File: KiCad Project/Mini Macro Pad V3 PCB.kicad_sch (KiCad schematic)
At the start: 0 parts

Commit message: added basic components & neopixels to schematic
just adding base components to schematic. not really any wiring yet
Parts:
- added D1, D10, D2, D3, D4, D5, D6, D7, D8, D9: NeoPixel_THT, symbol LED:NeoPixel_THT
- added J1: USB_C_Receptacle_USB2.0_14P, symbol Connector:USB_C_Receptacle_USB2.0_14P
- added U1: RP2040, Package_DFN_QFN:QFN-56-1EP_7x7mm_P0.4mm_EP3.2x3.2mm, symbol MCU_RaspberryPi:RP2040
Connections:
- new net: D8.1 (DOUT), D9.4 (DIN)
- new net: D7.1 (DOUT), D8.4 (DIN)
- new net: D2.1 (DOUT), D3.4 (DIN)
- new net: D1.1 (DOUT), D2.4 (DIN)
- new net: D10.1 (DOUT), D7.4 (DIN)
- new net: D4.1 (DOUT), D5.4 (DIN)
- new net: D3.1 (DOUT), D4.4 (DIN)
- new net: J1.A1 (GND), J1.A12 (GND), J1.B1 (GND), J1.B12 (GND)
- new net: J1.A4 (VBUS), J1.A9 (VBUS), J1.B4 (VBUS), J1.B9 (VBUS)
- new net: D10.4 (DIN), D6.1 (DOUT)
- new net: D5.1 (DOUT), D6.4 (DIN)
- new net: U1.1 (IOVDD), U1.10 (IOVDD), U1.22 (IOVDD), U1.33 (IOVDD), U1.42 (IOVDD), U1.49 (IOVDD)
- new net: U1.23 (DVDD), U1.50 (DVDD)
- new net GND: D1.2 (GND), D10.2 (GND), D2.2 (GND), D3.2 (GND), D4.2 (GND), D5.2 (GND), D6.2 (GND), D7.2 (GND), D8.2 (GND), D9.2 (GND)

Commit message: same thing as previous commit
https://datasheets.raspberrypi.com/rp2040/hardware-design-with-rp2040.pdf
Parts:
- added C1, C2: 10u, symbol Device:C
- added U2: NCP1117-3.3_SOT223, Package_TO_SOT_SMD:SOT-223-3_TabPin2, symbol Regulator_Linear:NCP1117-3.3_SOT223
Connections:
- net GND: now also J1.A1 (GND), J1.A12 (GND), J1.B1 (GND), J1.B12 (GND), J1.S1 (SHIELD), C1.2, C2.2, U2.1 (GND); no longer D9.2 (GND)
- net +3.3V: now reaches D8.3 (VDD)
- net +3.3V: now also D1.3 (VDD), D10.3 (VDD), D2.3 (VDD), D3.3 (VDD), D4.3 (VDD), D5.3 (VDD), D6.3 (VDD), D7.3 (VDD), D9.3 (VDD), U1.1 (IOVDD), U1.10 (IOVDD), U1.22 (IOVDD), U1.23 (DVDD), U1.33 (IOVDD), U1.42 (IOVDD), U1.43 (ADC_AVDD), U1.44 (VREG_IN), U1.45 (VREG_VOUT), U1.48 (USB_VDD), U1.49 (IOVDD), U1.50 (DVDD), C2.1, U2.2 (VO)
- net VBUS: now reaches J1.A4 (VBUS), J1.A9 (VBUS), J1.B4 (VBUS), J1.B9 (VBUS)
- net VBUS: now also C1.1, U2.3 (VI)
- net NeoPixel_DIN: now reaches D1.4 (DIN)
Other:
- note added: "USB & Power"
- title: (none) -> Mini Macro Pad V3
- moved on the sheet: D1, D10, D2, D3, D4, D5, D6, D7, D8, D9, J1, U1

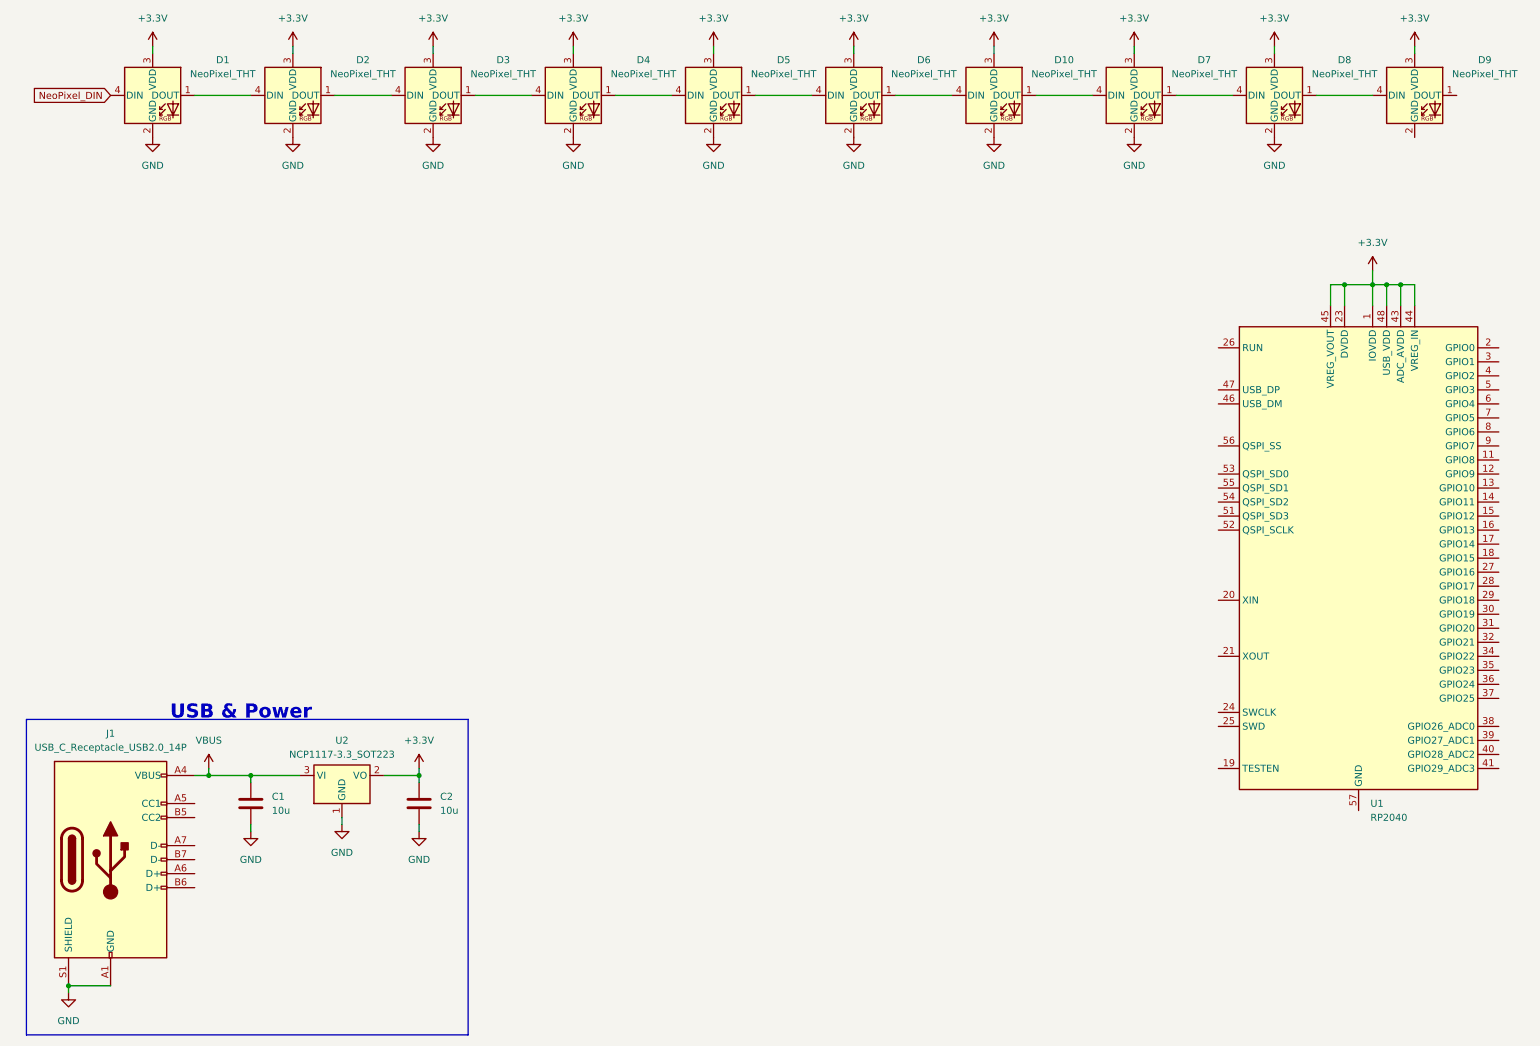
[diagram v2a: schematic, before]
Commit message: added flash to schematic
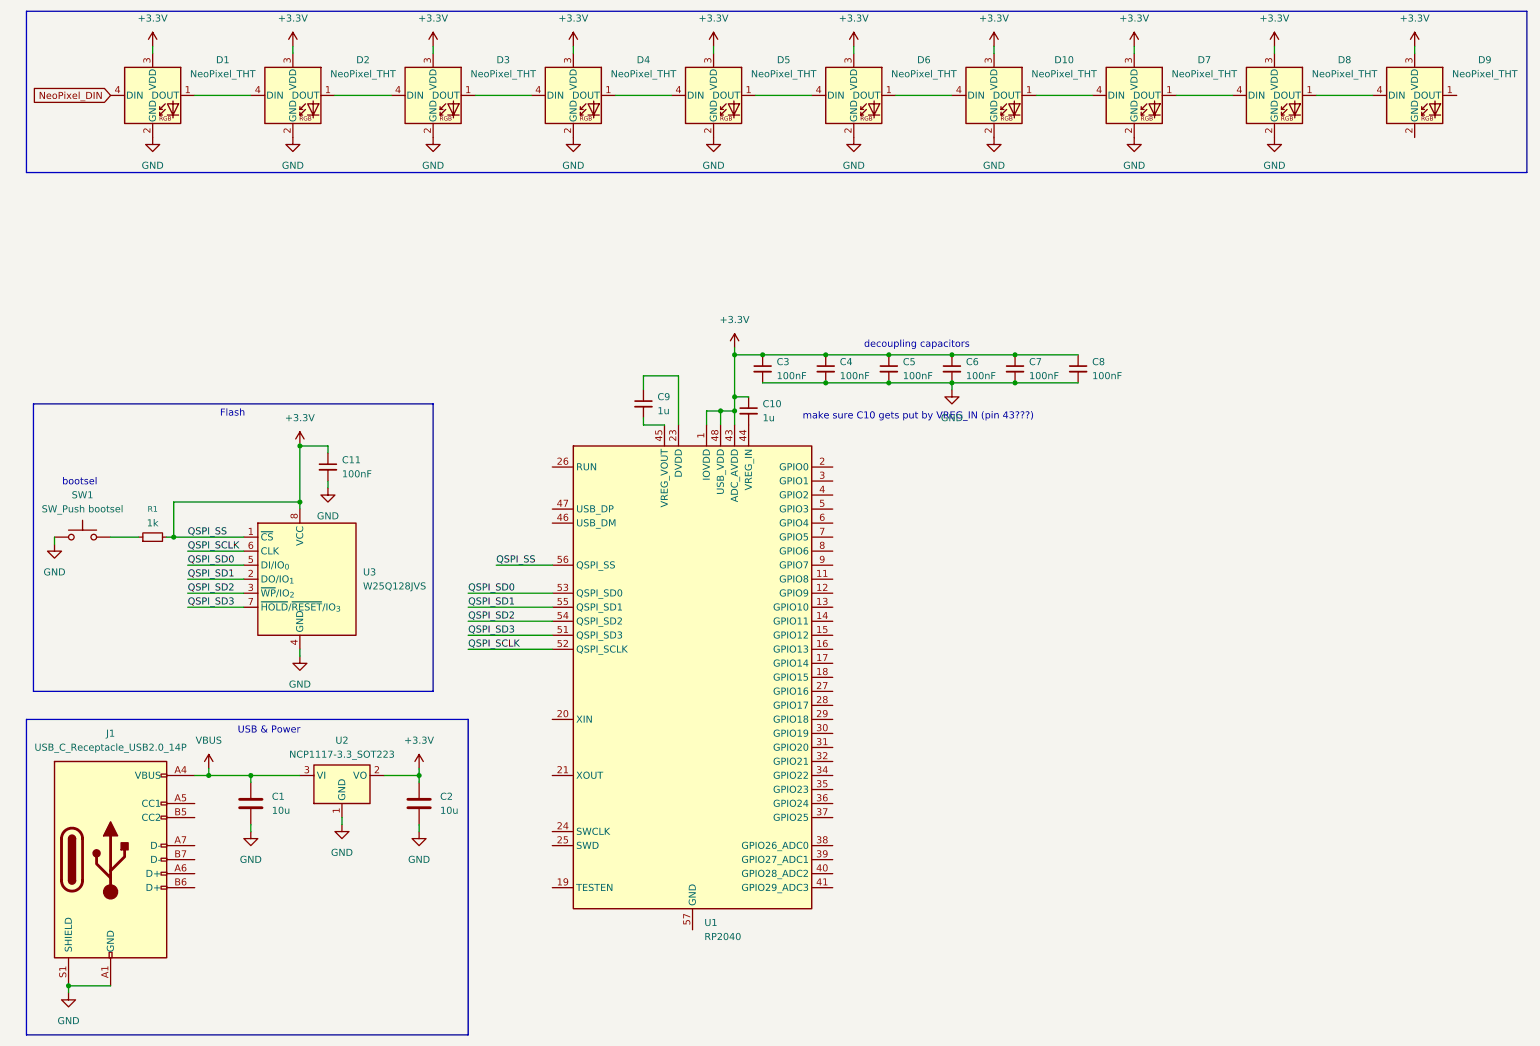
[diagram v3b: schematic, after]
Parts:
- added C10, C9: 1u, Capacitor_SMD:C_0402_1005Metric_Pad0.74x0.62mm_HandSolder, symbol Device:C_Small
- added C11, C3, C4, C5, C6, C7, C8: 100nF, symbol Device:C_Small
- added R1: 1k, symbol Device:R_Small
- added SW1: SW_Push bootsel, symbol Switch:SW_Push
- added U3: W25Q128JVS, Package_SO:SOIC-8_5.3x5.3mm_P1.27mm, symbol Memory_Flash:W25Q128JVS
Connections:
- net +3.3V: now also U1.56 (QSPI_SS), C10.1, C11.1, C3.1, C4.1, C5.1, C6.1, C7.1, C8.1, R1.2, U3.1 (~{CS}), U3.8 (VCC); no longer U1.23 (DVDD), U1.44 (VREG_IN), U1.45 (VREG_VOUT), U1.50 (DVDD)
- net GND: now also C11.2, C3.2, C4.2, C5.2, C6.2, C7.2, C8.2, SW1.1, U3.4 (GND)
- net QSPI_SD3: now reaches U1.51 (QSPI_SD3)
- net QSPI_SD3: now also U3.7 (~{HOLD}/~{RESET}/IO_{3})
- net QSPI_SCLK: now reaches U1.52 (QSPI_SCLK)
- net QSPI_SCLK: now also U3.6 (CLK)
- net QSPI_SD0: now reaches U1.53 (QSPI_SD0)
- net QSPI_SD0: now also U3.5 (DI/IO_{0})
- net QSPI_SD2: now reaches U1.54 (QSPI_SD2)
- net QSPI_SD2: now also U3.3 (~{WP}/IO_{2})
- net QSPI_SD1: now reaches U1.55 (QSPI_SD1)
- net QSPI_SD1: now also U3.2 (DO/IO_{1})
- new net: R1.1, SW1.2
- new net: C10.2, U1.44 (VREG_IN)
- new net: C9.1, U1.23 (DVDD), U1.50 (DVDD)
- new net: C9.2, U1.45 (VREG_VOUT)
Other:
- note added: "Flash"
- note added: "bootsel"
- note added: "decoupling capacitors"
- note added: "make sure C10 gets put by VREG_IN (pin 43???)"
- moved on the sheet: U1

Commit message: added crystal to schematic
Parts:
- added C12, C13: 15P, symbol Device:C_Small
- added R2: 1k, symbol Device:R_Small
- added Y1: Crystal_GND24, symbol Device:Crystal_GND24
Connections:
- net GND: now also C12.1, C13.1, Y1.2, Y1.4
- net XIN: now reaches U1.20 (XIN)
- net XIN: now also C12.2, Y1.1
- net XOUT: now reaches U1.21 (XOUT)
- net XOUT: now also C13.2, R2.1, R2.2
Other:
- note added: "Crystal"
- moved on the sheet: C10, C11, C3, C4, C5, C6, C7, C8, C9, R1, SW1, U1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

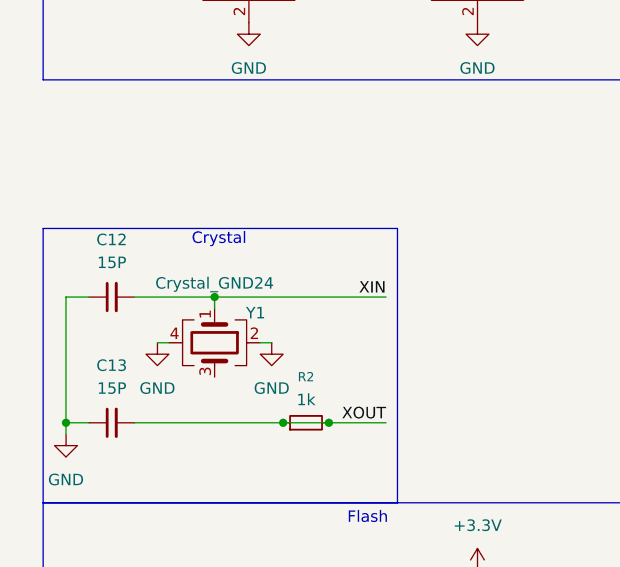
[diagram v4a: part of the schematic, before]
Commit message: added footprint for crystal
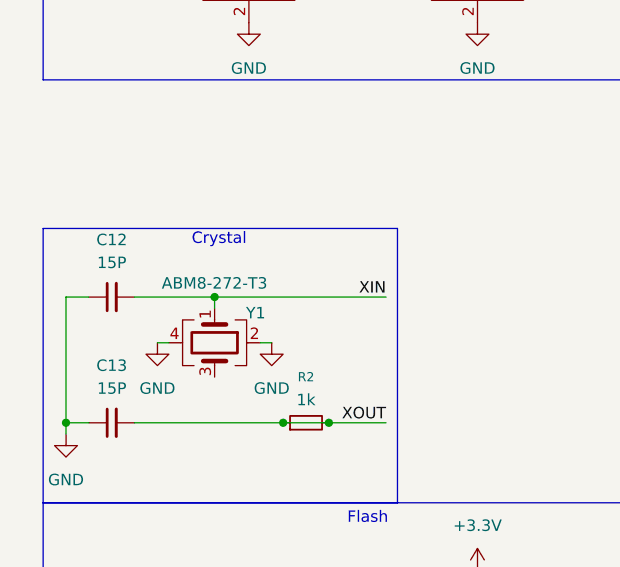
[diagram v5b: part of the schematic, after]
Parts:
- Y1: value Crystal_GND24 -> ABM8-272-T3; footprint (none) -> Custom Footprints:ABM8-272-T3_ABR
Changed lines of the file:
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@@
 			)
 		)
-		(property "Value" "Crystal_GND24"
+		(property "Value" "ABM8-272-T3"
 			(at 31.75 64.516 90)
 			(do_not_autoplace yes)
@@
 			)
 		)
-		(property "Footprint" ""
+		(property "Footprint" "Custom Footprints:ABM8-272-T3_ABR"
 			(at 31.75 71.12 0)
 			(effects

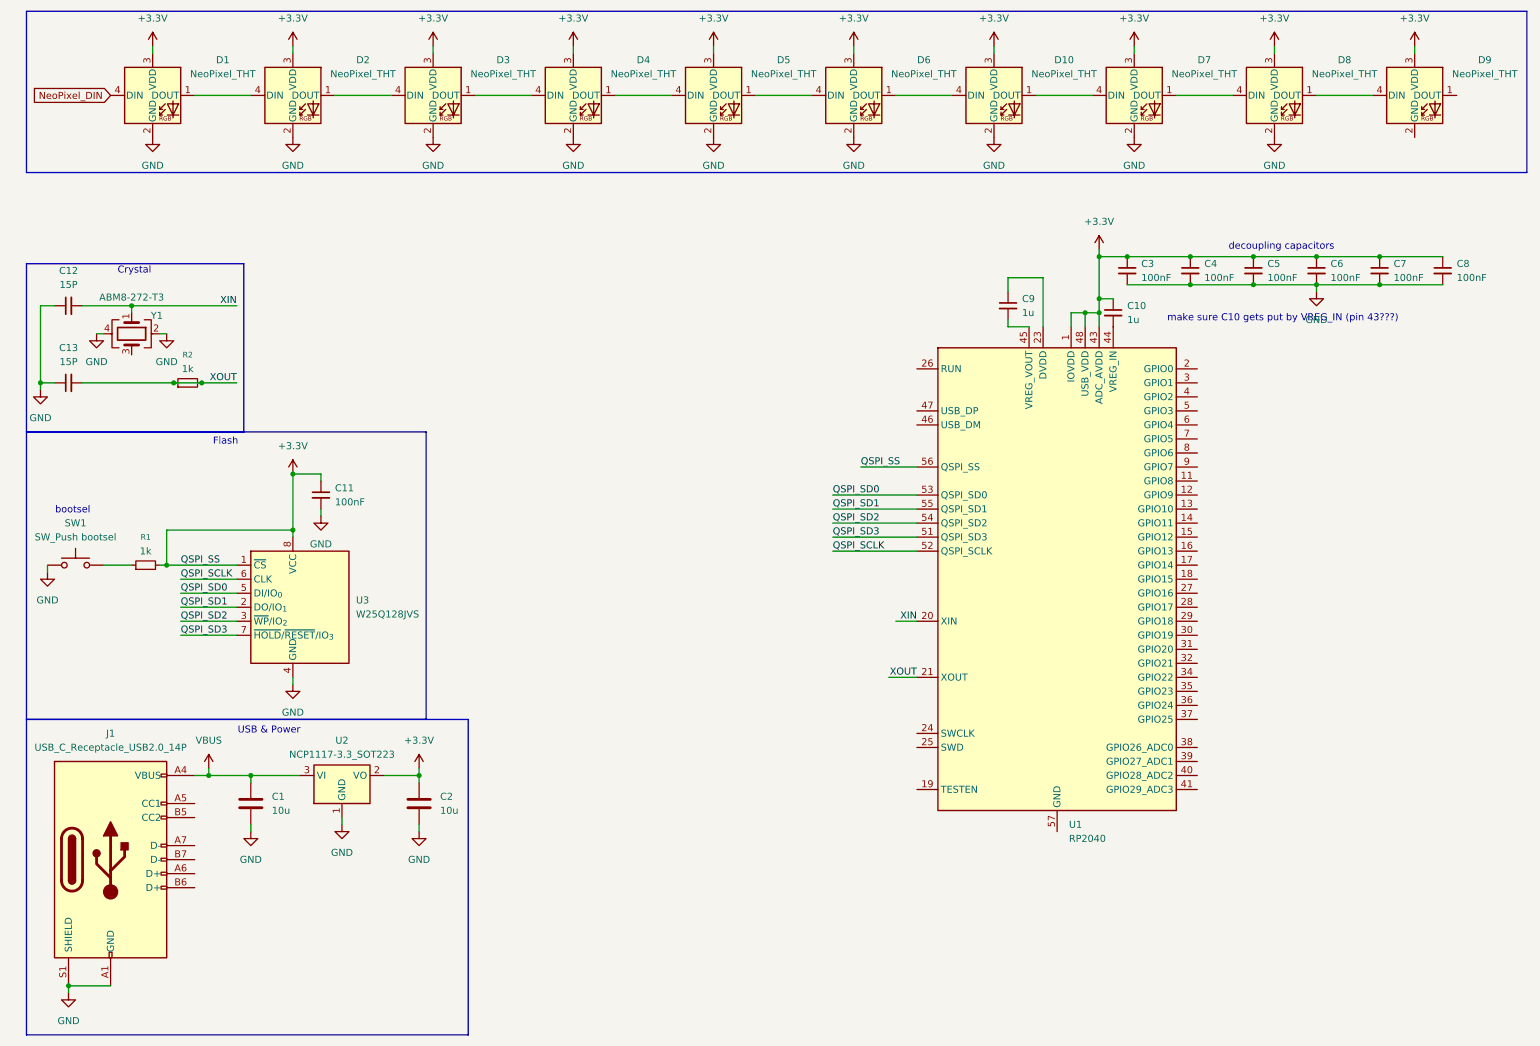
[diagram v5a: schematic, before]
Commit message: added button matrix
button matrix columns are connected to GPIO 0 to GPIO 3 rows are connected to GPIO 4 to GPIO 8
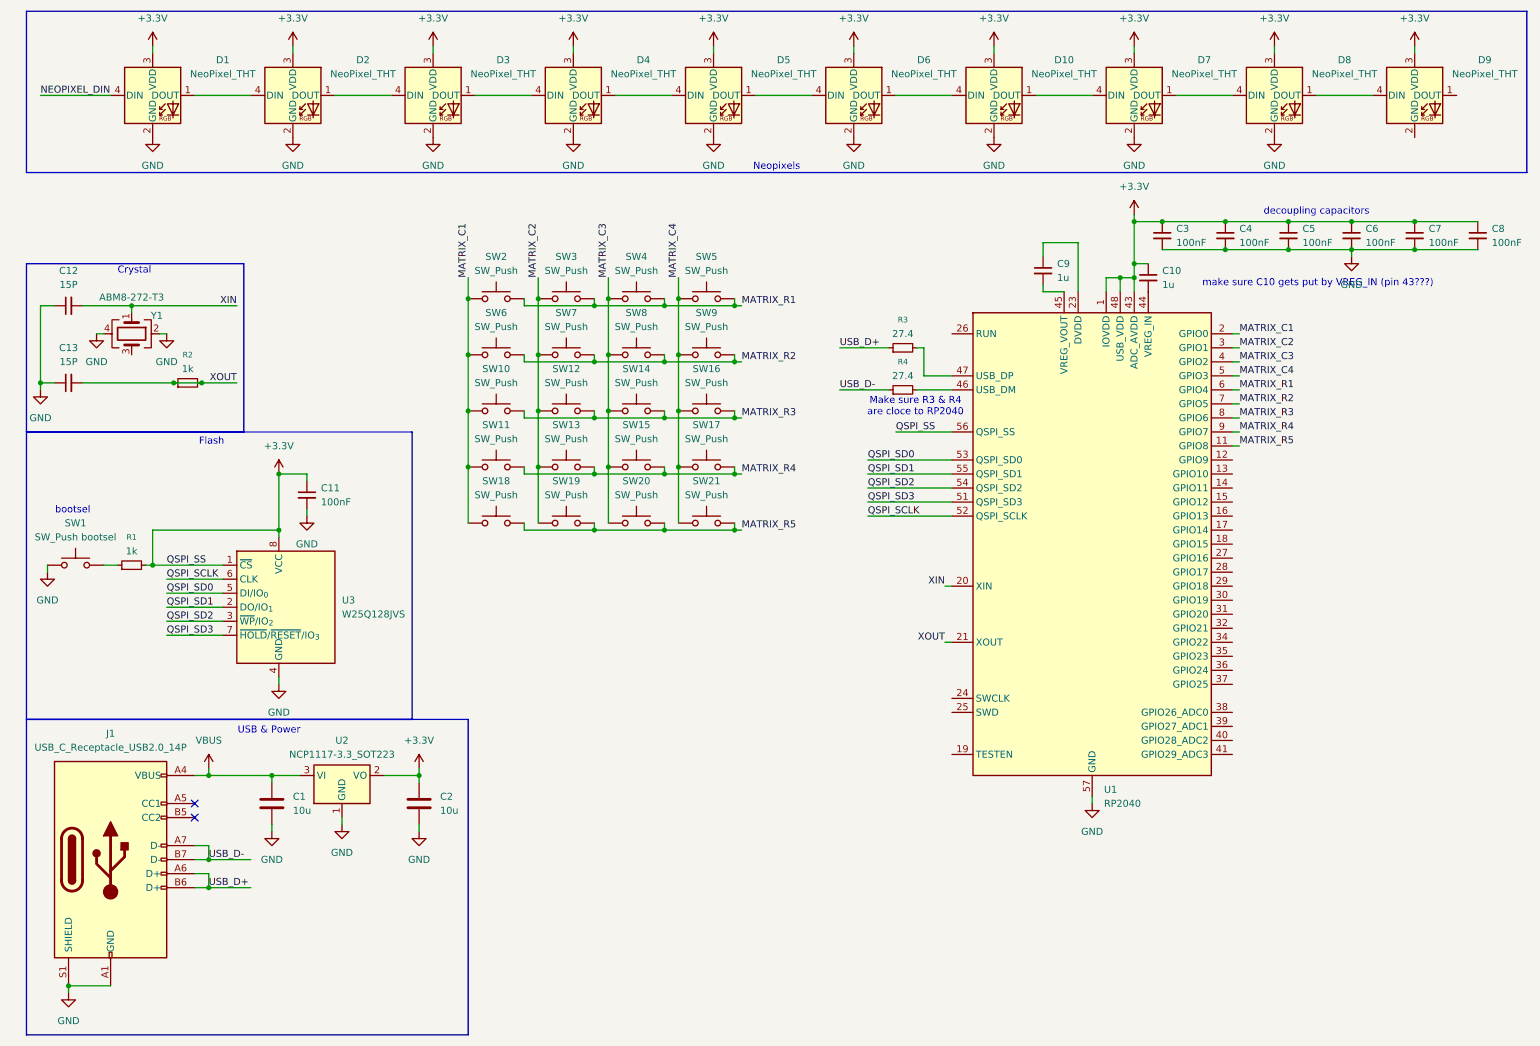
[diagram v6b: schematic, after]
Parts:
- added R3, R4: 27.4, symbol Device:R_Small
- added SW10, SW11, SW12, SW13, SW14, SW15, SW16, SW17, SW18, SW19, SW2, SW20, SW21, SW3, SW4, SW5, SW6, SW7, SW8, SW9: SW_Push, symbol Switch:SW_Push
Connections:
- net GND: now also U1.57 (GND)
- net USB_D+: now reaches J1.A6 (D+)
- net USB_D+: now also J1.B6 (D+), R3.1
- net USB_D-: now reaches J1.A7 (D-)
- net USB_D-: now also J1.B7 (D-), R4.1
- net MATRIX_R5: now reaches U1.11 (GPIO8)
- net MATRIX_R5: now also SW18.2, SW19.2, SW20.2, SW21.2
- net MATRIX_C1: now reaches U1.2 (GPIO0)
- net MATRIX_C1: now also SW10.1, SW11.1, SW18.1, SW2.1, SW6.1
- net MATRIX_C2: now reaches U1.3 (GPIO1)
- net MATRIX_C2: now also SW12.1, SW13.1, SW19.1, SW3.1, SW7.1
- net MATRIX_C3: now reaches U1.4 (GPIO2)
- net MATRIX_C3: now also SW14.1, SW15.1, SW20.1, SW4.1, SW8.1
- net at U1.46 (USB_DM): now also R4.2
- net at U1.47 (USB_DP): now also R3.2
- net MATRIX_C4: now reaches U1.5 (GPIO3)
- net MATRIX_C4: now also SW16.1, SW17.1, SW21.1, SW5.1, SW9.1
- net MATRIX_R1: now reaches U1.6 (GPIO4)
- net MATRIX_R1: now also SW2.2, SW3.2, SW4.2, SW5.2
- net MATRIX_R2: now reaches U1.7 (GPIO5)
- net MATRIX_R2: now also SW6.2, SW7.2, SW8.2, SW9.2
- net MATRIX_R3: now reaches U1.8 (GPIO6)
- net MATRIX_R3: now also SW10.2, SW12.2, SW14.2, SW16.2
- net MATRIX_R4: now reaches U1.9 (GPIO7)
- net MATRIX_R4: now also SW11.2, SW13.2, SW15.2, SW17.2
- net NeoPixel_DIN renamed NEOPIXEL_DIN
- no-connect marks 0 -> 2
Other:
- note added: "Make sure R3 & R4 are cloce to RP2040"
- note added: "Neopixels"
- moved on the sheet: C1, C10, C11, C3, C4, C5, C6, C7, C8, C9, R1, U1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

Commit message: added rotary encoders
connected to GPIO 10 to GPIO 15
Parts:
- added SW22, SW23: RotaryEncoder_Switch_MP, symbol Device:RotaryEncoder_Switch_MP
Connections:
- net GND: now also SW22.C, SW22.MP, SW22.S2, SW23.C, SW23.MP, SW23.S2
- net NEOPIXEL_DIN: now also U1.12 (GPIO9)
- net ENCODER_1_A: now reaches U1.13 (GPIO10)
- net ENCODER_1_A: now also SW22.A
- net ENCODER_1_B: now reaches U1.14 (GPIO11)
- net ENCODER_1_B: now also SW22.B
- net ENCODER_1_S1: now reaches U1.15 (GPIO12)
- net ENCODER_1_S1: now also SW22.S1
- net ENCODER_2_A: now reaches U1.16 (GPIO13)
- net ENCODER_2_A: now also SW23.A
- net ENCODER_2_B: now reaches U1.17 (GPIO14)
- net ENCODER_2_B: now also SW23.B
- net ENCODER_2_S1: now reaches U1.18 (GPIO15)
- net ENCODER_2_S1: now also SW23.S1
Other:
- note added: "Button Matrix"
- note added: "Rotary Encoders"
- moved on the sheet: SW10, SW11, SW12, SW13, SW14, SW15, SW16, SW17, SW18, SW19, SW2, SW20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
